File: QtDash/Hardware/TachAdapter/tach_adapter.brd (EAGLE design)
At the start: 43.5 x 14 mm, 10 parts, among them IC1 TLP293

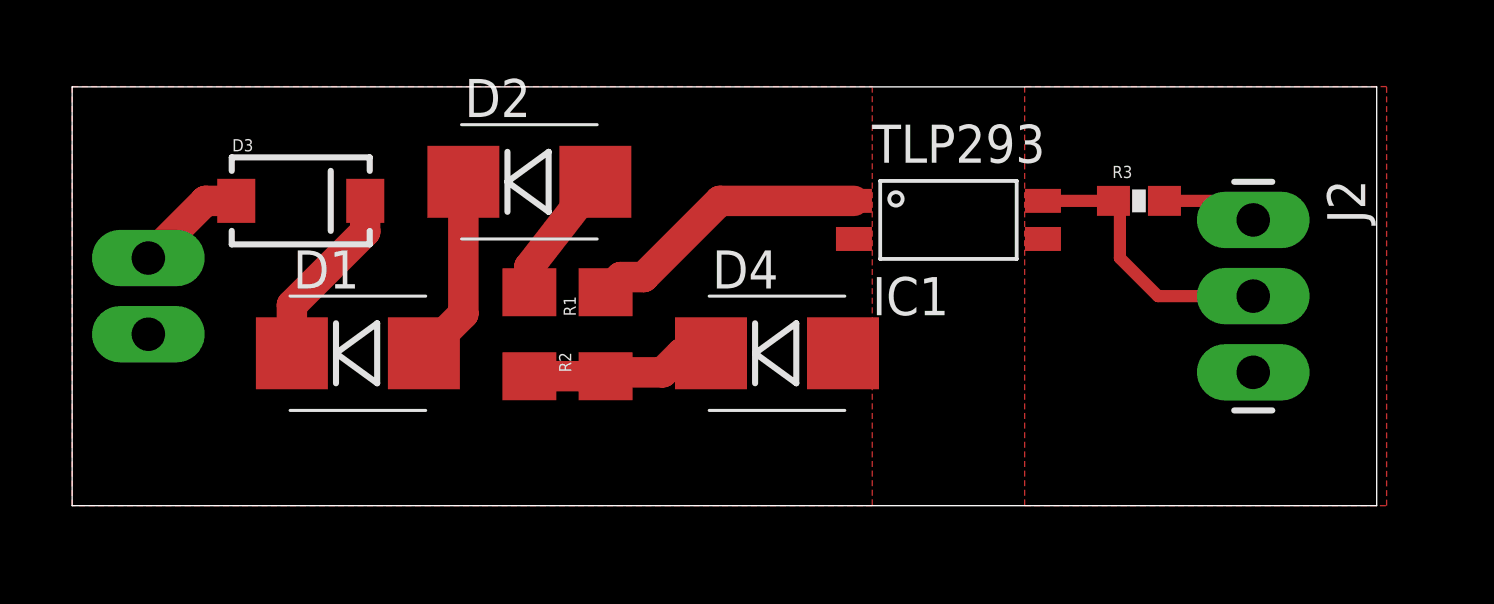
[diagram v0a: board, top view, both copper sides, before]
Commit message: - updated tach adapter with opto-coupler that is currently available 	- added datasheets for tach-adapter components 	- updated dashhat library with new connector 31 dimensions 	- moved circuit simulations into their own folder
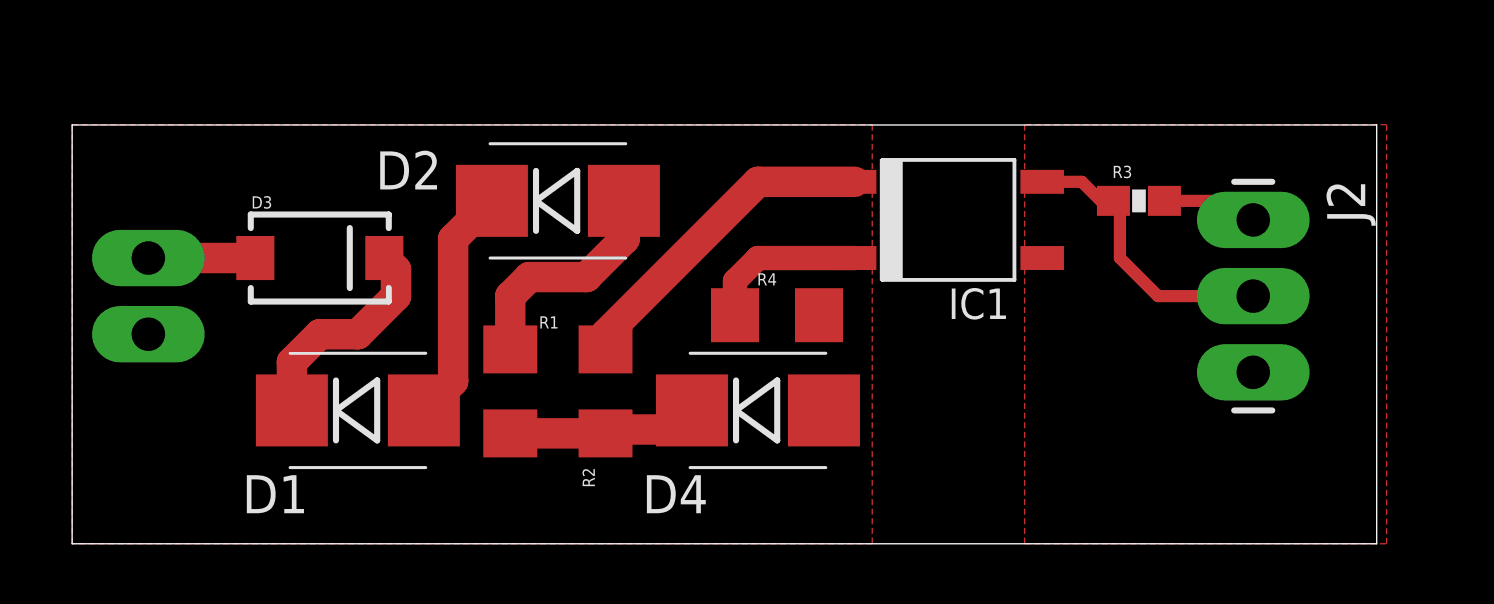
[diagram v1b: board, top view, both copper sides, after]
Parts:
- added R4: 220, SparkFun-Passives:1206
- D1, D2: value DIODE-ZENERSMB -> 82V
- D4: value DIODE-ZENERSMB -> 13V
- IC1: value TLP293 -> PS2701-1; device tach_adapter:SO4 -> tach_adapter:4-SMD
- R2: value 0 -> 220
- moved D4 2.01 mm to (22.9, 3.17)
- moved R1 2.01 mm to (14.6, 3.81)
- moved D3 2.01 mm to (8.26, 8.26)
- moved D1 1.91 mm to (9.53, 3.17)
- moved R2 1.90 mm to (17.8, 3.81)
- moved D2 1.14 mm to (16.2, 10.2)
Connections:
- new net N$6: IC1.2, R4.2
- net GND-ISO: now also R4.1; no longer IC1.2
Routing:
- net N$6: track 0.00 -> 5.45 mm
- net N$3: track 4.43 -> 7.65 mm
- net N$2: track 6.26 -> 7.94 mm
- net N$5: track 9.54 -> 10.9 mm
- net N$1: track 6.09 -> 7.42 mm

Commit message: - finished tach adapter board -- ordered components and board from OSHPark
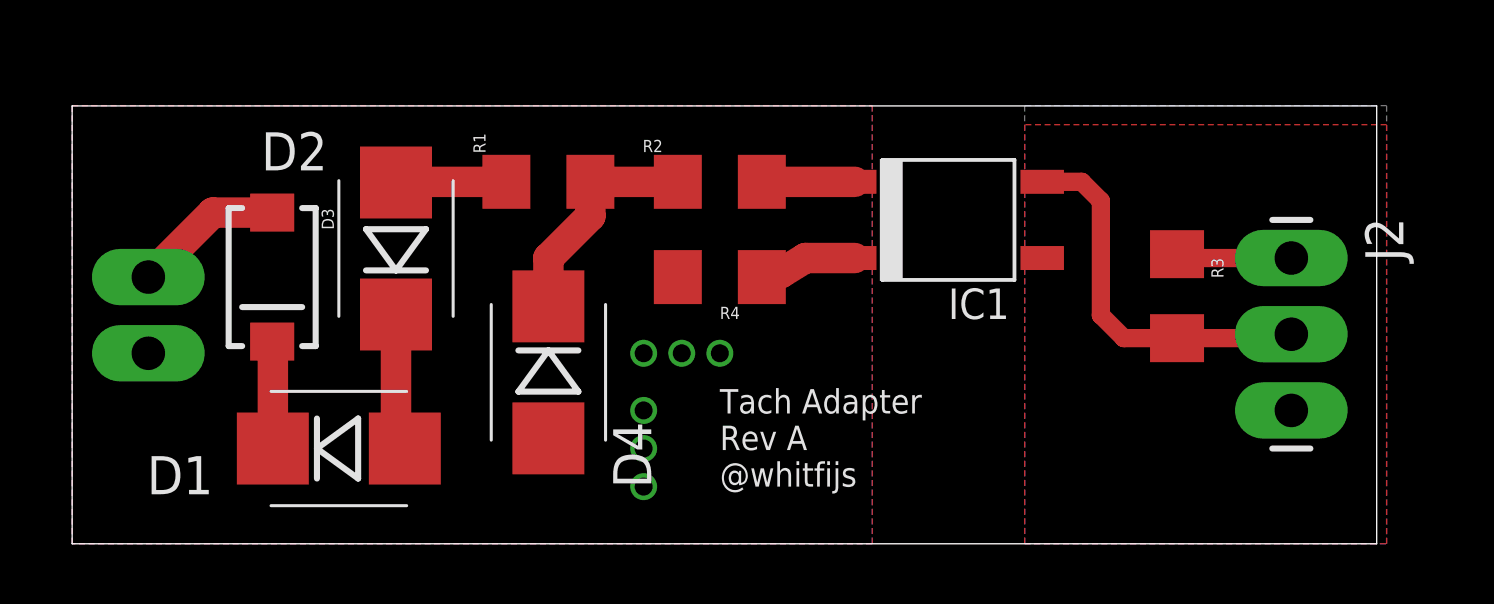
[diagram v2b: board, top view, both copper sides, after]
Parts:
- R3: device SparkFun-Passives:0603-RES -> SparkFun-Passives:1206
- moved R2 7.96 mm to (21.6, 10.8), turned to 0 degrees
- moved D4 7.10 mm to (15.9, 4.45), turned to 270 degrees
- moved R1 7.10 mm to (15.9, 10.8), turned to 0 degrees
- moved D2 5.63 mm to (10.8, 8.57), turned to 90 degrees
- moved R3 3.42 mm to (36.8, 6.99), turned to 270 degrees
- moved R4 2.29 mm to (21.6, 7.62), turned to 0 degrees
- moved J2 1.80 mm to (40.6, 8.26)
- moved D3 1.71 mm to (6.67, 7.62), turned to 270 degrees
- moved D1 1.42 mm to (8.89, 1.91)
- moved J1 0.63 mm to (2.54, 5.08)
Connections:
- net 3.3V: now also R3.1; no longer R3.2
- net N$7: now also R3.2; no longer R3.1
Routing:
- net N$5: track 10.9 -> 3.10 mm
- net N$1: track 7.42 -> 3.57 mm
- net N$3: track 7.65 -> 3.80 mm
- net N$2: track 7.94 -> 4.59 mm
- net N$7: track 9.60 -> 12.7 mm
- net N$6: track 5.45 -> 3.25 mm
- net N$8: track 3.57 -> 5.02 mm
- net N$4: track 6.37 -> 7.64 mm
- net 3.3V: track 3.22 -> 3.86 mm
- added copper zone on layer 16, net GND
- added copper zone on layer 16, net GND-ISO
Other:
- board size 43.5 x 14 mm -> 43.5 x 14.6 mm
- board text added: "Tach Adapter Rev A @whitfijs"

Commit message: bugfix/hardware-revA-issues 	- removed superfluous zener diodes from input of tach adapter board 	- changed input/output wire solder hole sizes 	- added debouncing circuit that probably won't work on the output.
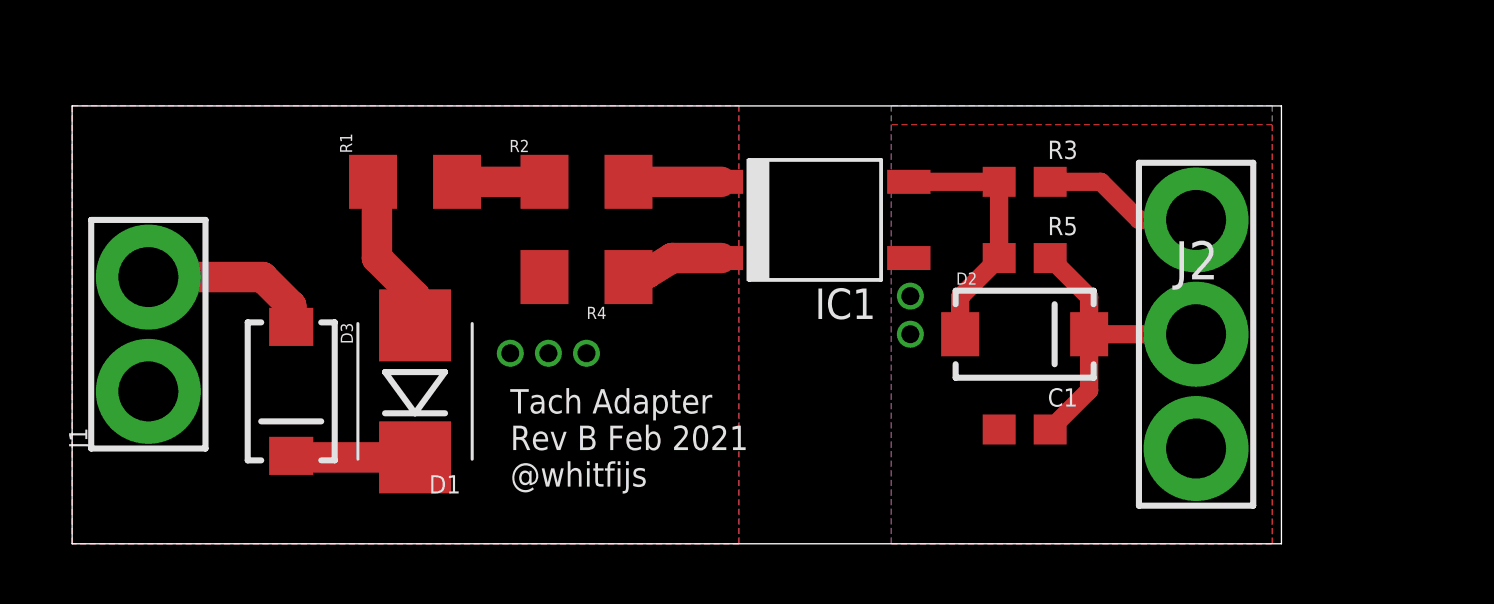
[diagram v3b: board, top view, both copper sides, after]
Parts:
- removed D4: 13V, SparkFun-DiscreteSemi:SMB-DIODE
- added C1: 10n, digital_dash:0603
- added R5: 1k, digital_dash:0603
- D1: value 82V -> 13V
- D2: value 82V -> (none); device SparkFun-DiscreteSemi:SMB-DIODE -> SparkFun-DiscreteSemi:SMA-DIODE
- J1: device SparkFun-Connectors:1X02_LONGPADS -> digital_dash:1X02_LARGE
- J2: device SparkFun-Connectors:1X03_LONGPADS -> digital_dash:1X03_LARGE
- R3: device SparkFun-Passives:1206 -> digital_dash:0603
- moved D2 21.1 mm to (31.8, 5.71), turned to 0 degrees
- moved R3 6.35 mm to (31.8, 10.8), turned to 180 degrees
- moved IC1 4.45 mm to (24.8, 9.53)
- moved R1 4.45 mm to (11.4, 10.8)
- moved R2 4.45 mm to (17.1, 10.8)
- moved R4 4.45 mm to (17.1, 7.62)
- moved J2 4.07 mm to (37.5, 5.71)
- moved D3 3.86 mm to (7.30, 3.81)
- moved D1 3.17 mm to (11.4, 3.81), turned to 90 degrees
- moved J1 1.27 mm to (2.54, 6.35)
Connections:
- net GND: now also C1.2
- net GND-ISO: no longer D4.A
- net N$2: now also C1.1, J2.2, R5.2; no longer D1.A
- net N$3: now also D1.A; no longer D2.A
- net N$4: no longer D4.C
- net N$7: now also D2.A, R5.1; no longer J2.2
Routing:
- net N$2: track 4.59 -> 10.4 mm
- net N$4: track 7.64 -> 2.91 mm
- net N$7: track 12.7 -> 8.63 mm
- net N$3: track 3.80 -> 5.36 mm
- net 3.3V: track 3.86 -> 5.39 mm
- net N$8: track 5.02 -> 5.86 mm
- net N$1: track 3.57 -> 4.15 mm
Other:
- board size 43.5 x 14.6 mm -> 40.3 x 14.6 mm
- board text added: "Tach Adapter Rev B Feb 2021 @whitfijs"
- board text removed: "Tach Adapter Rev A @whitfijs"

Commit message: bugfix/tach-adapter-updates: 	- updated eagle tach adapter project
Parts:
- added C2: 100n, digital_dash:0603
- IC1: value PS2701-1 -> H11L1SR2VM; device tach_adapter:4-SMD -> tach_adapter:6-SMD
- moved R3 5.12 mm to (36.8, 10.2)
- moved C1 5.08 mm to (36.8, 2.54)
- moved D2 5.08 mm to (36.8, 5.71)
- moved J2 5.08 mm to (42.5, 5.71)
- moved R5 5.08 mm to (36.8, 8.26)
- moved IC1 1.80 mm to (26.0, 8.26)
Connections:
- net 3.3V: now also C2.1, IC1.6
- net GND: now also C2.2, IC1.5; no longer IC1.3
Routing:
- net 3.3V: track 5.39 -> 14.9 mm
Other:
- board size 40.3 x 14.6 mm -> 45.4 x 14.6 mm
